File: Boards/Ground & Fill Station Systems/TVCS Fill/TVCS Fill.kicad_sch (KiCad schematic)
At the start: 109 parts, among them J1 Conn_01x01_Socket, J10 Conn_01x01_Socket, J11 Conn_01x01_Socket, J12 Conn_01x01_Socket, J13 Conn_01x01_Socket, J14 Conn_01x01_Socket, J15 Conn_01x01_Socket, J17 XT30UPB-M, J2 Conn_01x01_Socket, J3 XT30UPB-M, J4 XT30UPB-M, J5 Conn_01x01_Socket, J6 XT30UPB-M, J8 Conn_01x01_Socket, J9 Conn_01x01_Socket, Q1 2N7002H6327XTSA2, U1 MAX31856MUD+T, U10 MAX31856MUD+T, U11 IRLZ44NPBF, U12 IRLZ44NPBF, U13 LM61460AASQRJRRQ1, U14 ADS1114IRUGR, U15 TPS1120DR, U16 IRLZ44NPBF, U17 MAX485CSA+T, U3 MAX31856MUD+T, U4 PCA9306DP_118, U5 MCP9808T-E/MC, U8 TPS1120DR, U9 LM61460AASQRJRRQ1

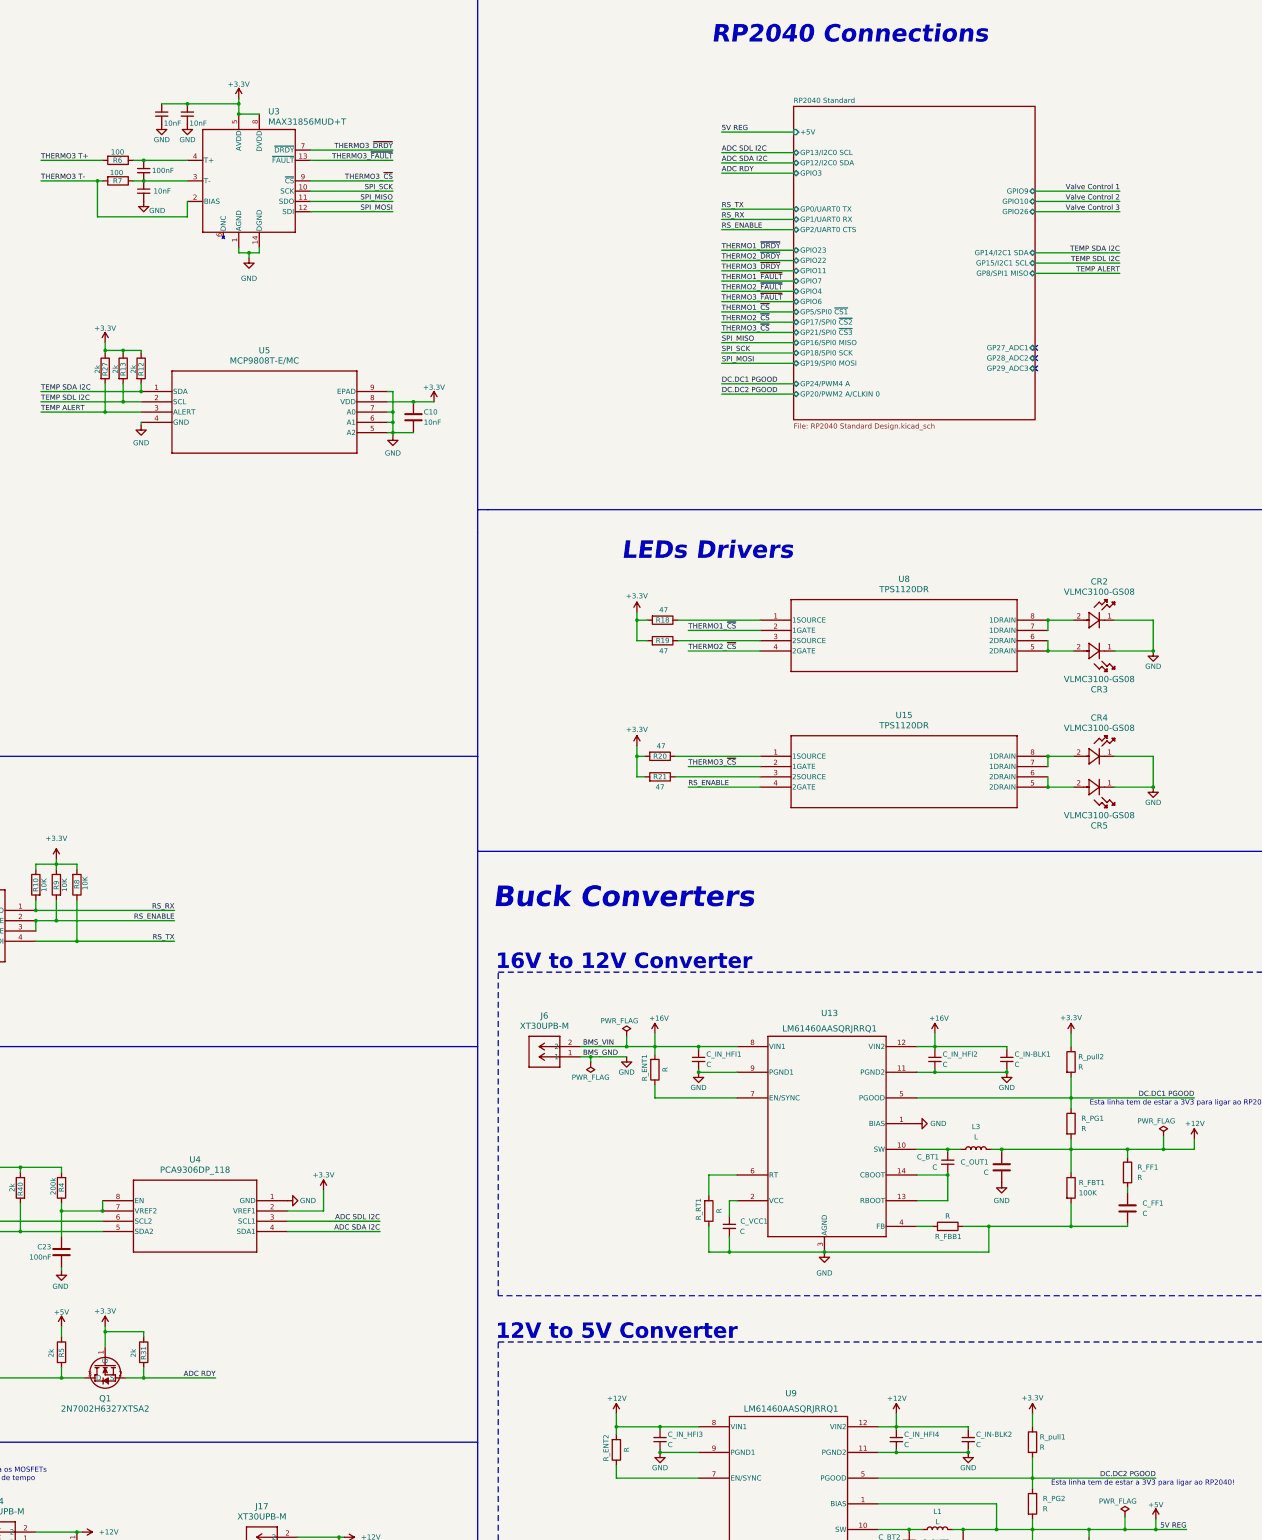
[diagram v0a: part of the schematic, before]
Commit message: Led driver circuit correction & RF FEM implementation
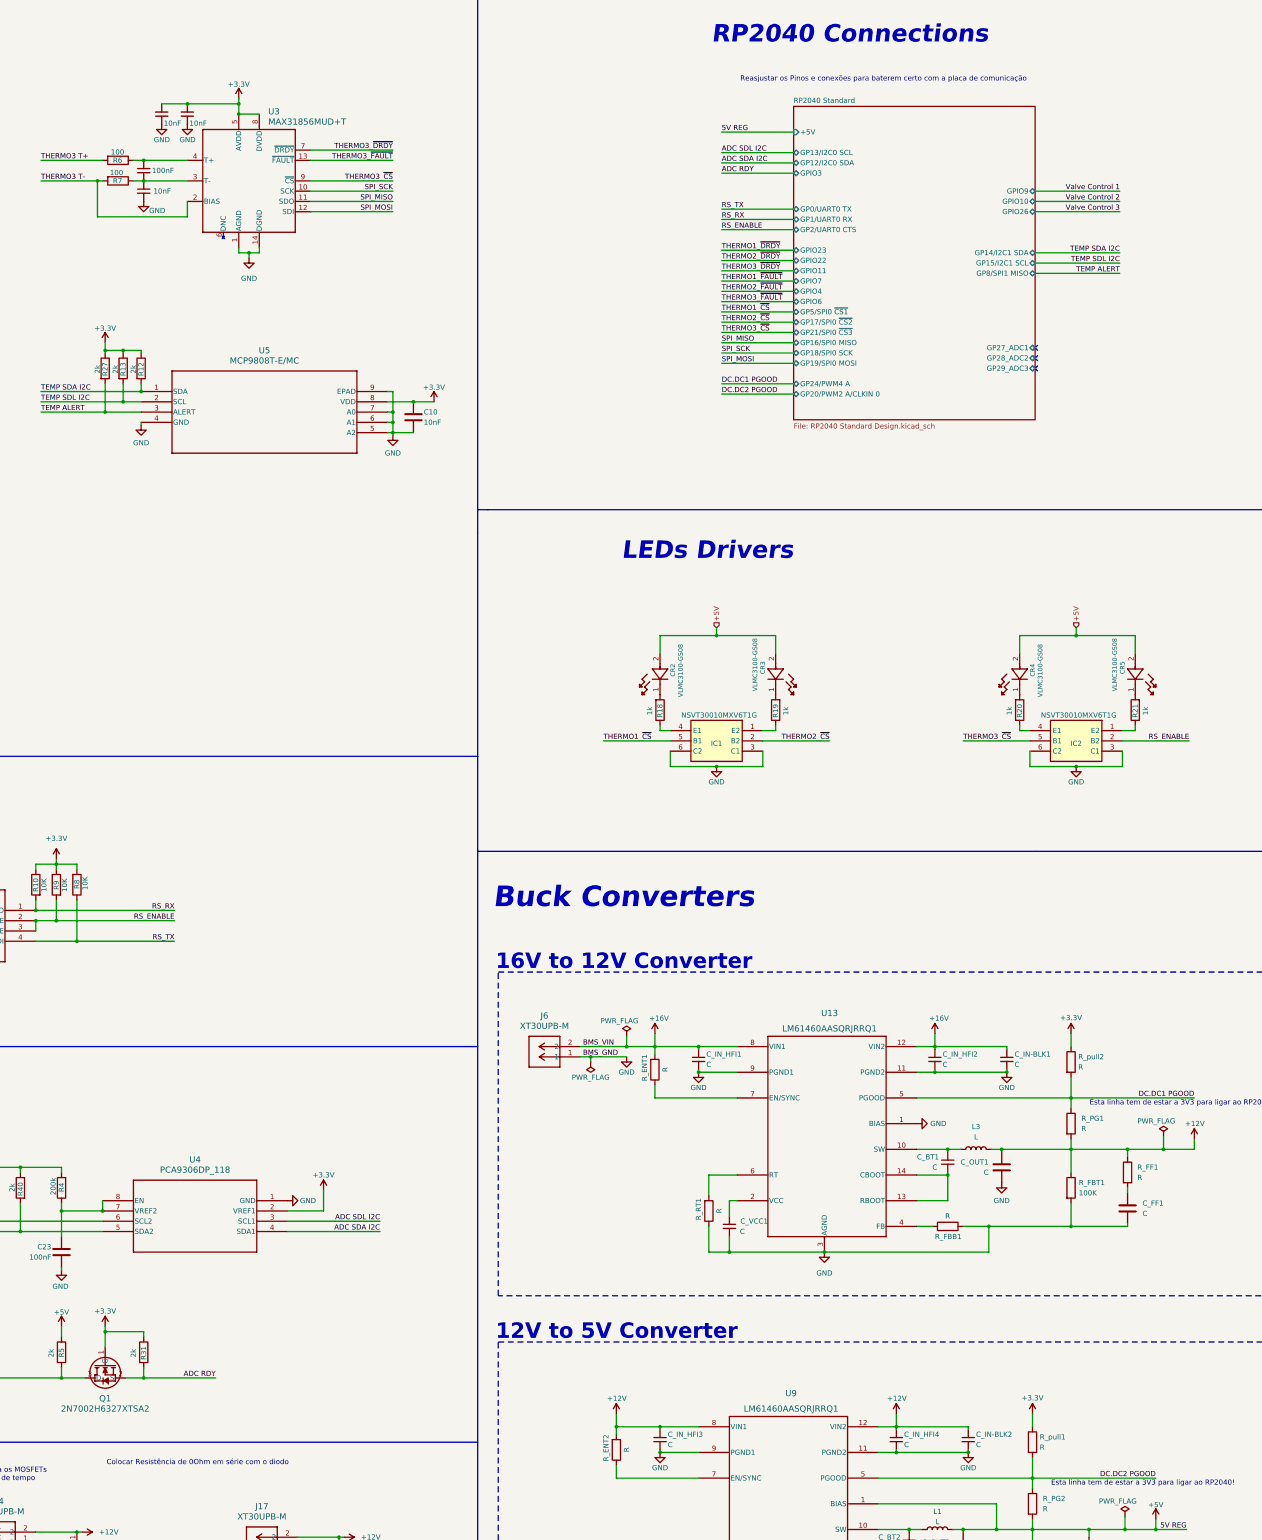
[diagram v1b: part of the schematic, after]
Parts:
- removed U15, U8: TPS1120DR, D8, symbol TPS1120DR:TPS1120DR
- added IC1, IC2: NSVT30010MXV6T1G, SOTFL50P160X60-6N, symbol NSVT30010MXV6T1G:NSVT30010MXV6T1G
- R18, R19, R20, R21: value 47 -> 1k; footprint RES_0402:RES_0402 -> RC0402N_VIS:RC0402N_VIS
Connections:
- net +3.3V: no longer R18.2, R19.2, R20.2, R21.2
- net +5V: now also CR2.2, CR3.2, CR4.2, CR5.2
- net GND: now also IC1.3 (C1), IC1.6 (C2), IC2.3 (C1), IC2.6 (C2); no longer CR2.1, CR3.1, CR4.1, CR5.1
- net RS_ENABLE: now also IC2.2 (B2)
- net THERMO1_~{CS}: now also IC1.5 (B1)
- net THERMO2_~{CS}: now also IC1.2 (B2)
- net THERMO3_~{CS}: now also IC2.5 (B1)
- net at R19.1: now also IC1.1 (E2)
- net at R21.1: now also IC2.1 (E2)
- net at R20.1: now also IC2.4 (E1)
- net at R18.1: now also IC1.4 (E1)
- new net: CR2.1, R18.2
- new net: CR3.1, R19.2
- new net: CR5.1, R21.2
- new net: CR4.1, R20.2
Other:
- note added: "Colocar Resistência de 0Ohm em série com o diodo"
- note added: "Reasjustar os Pinos e conexões para baterem certo com a placa de comunicação"

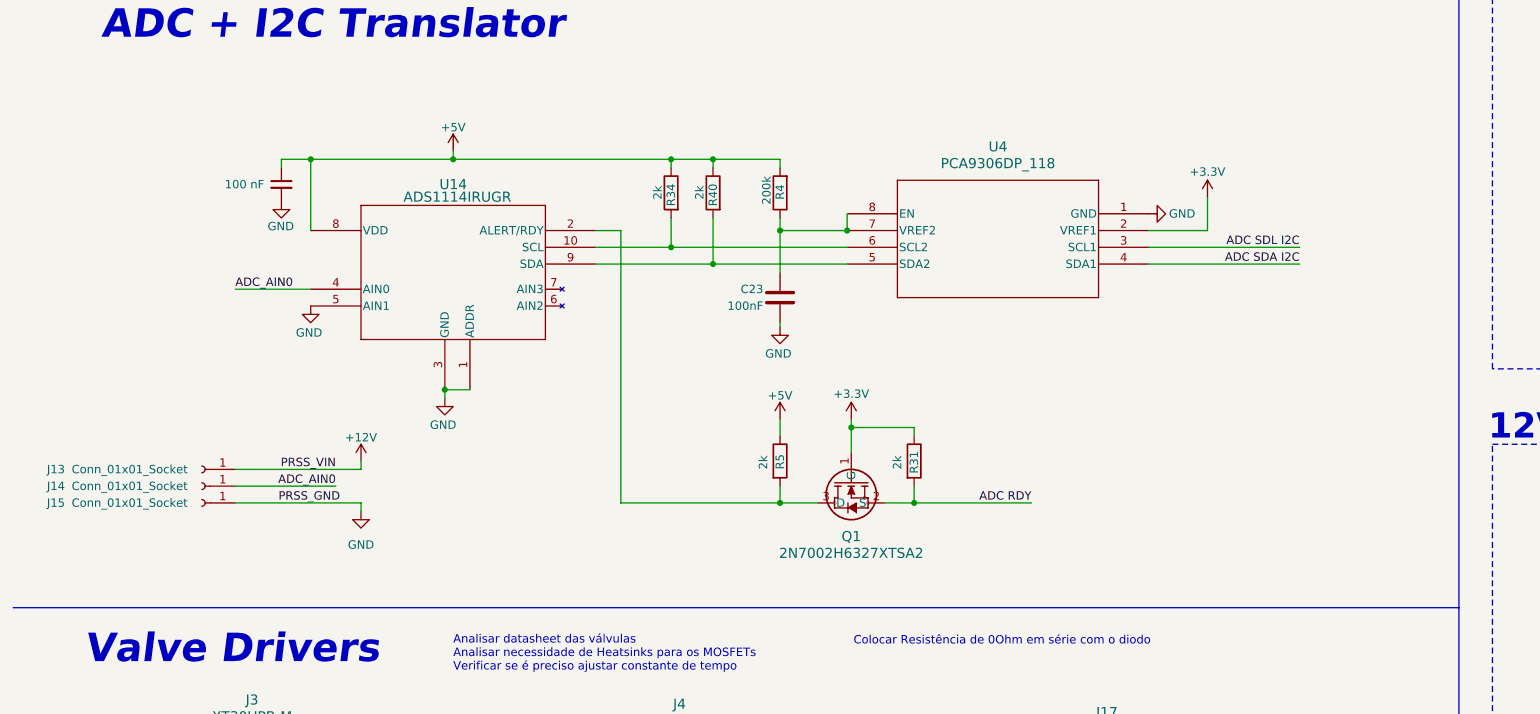
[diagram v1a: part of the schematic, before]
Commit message: ADS1115 implementation
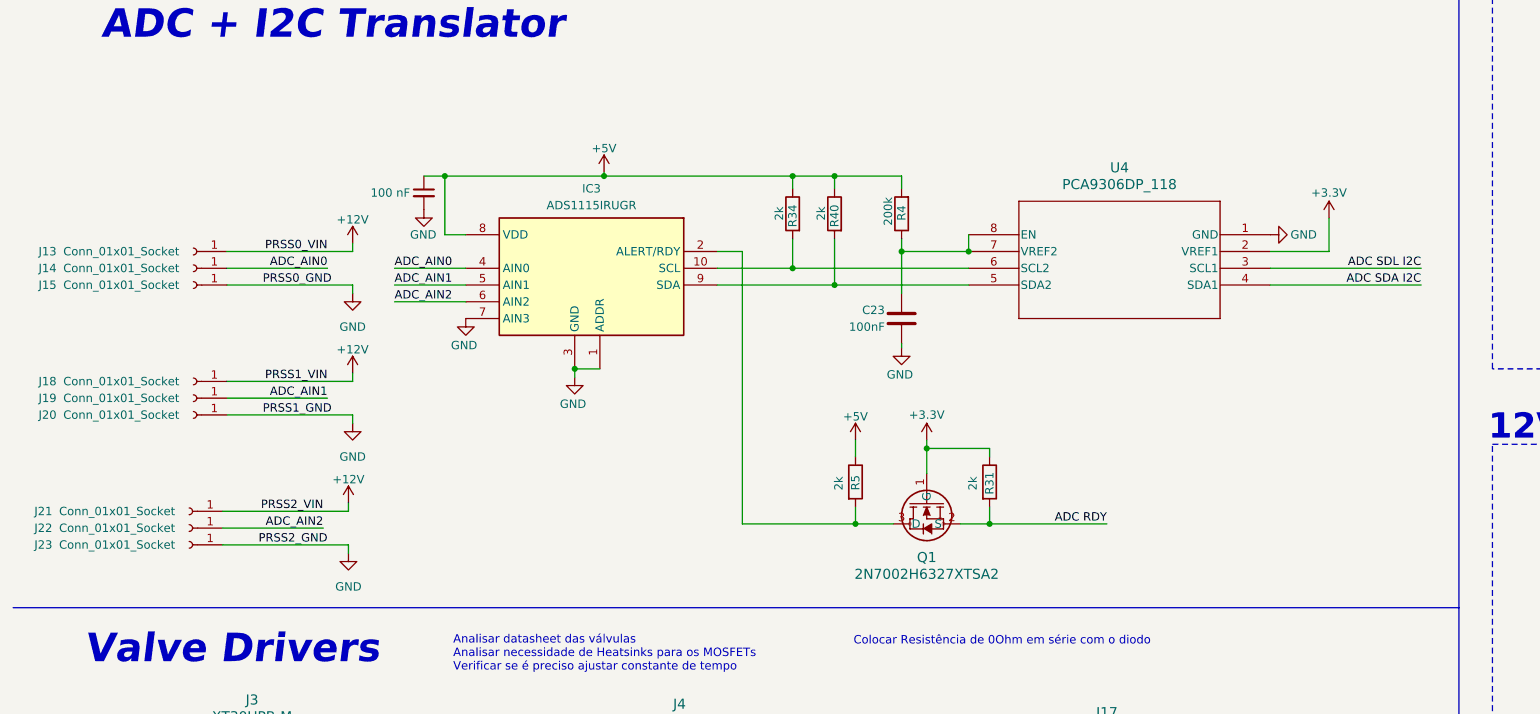
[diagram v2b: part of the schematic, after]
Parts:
- removed U14: ADS1114IRUGR, RUG10, symbol ADS1114:ADS1114IRUGR
- added IC3: ADS1115IRUGR, ADS1115IRUGR, symbol ADS1115IRUGR:ADS1115IRUGR
- added J18, J19, J20, J21, J22, J23: Conn_01x01_Socket, Button_Switch_THT:SW_Lever_1P2T_NKK_GW12LxH, symbol Connector:Conn_01x01_Socket
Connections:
- net +12V: now also J18.1 (Pin_1), J21.1 (Pin_1)
- net +5V: now also IC3.8 (VDD)
- net ADC_AIN0: now also IC3.4 (AIN0)
- net GND: now also IC3.1 (ADDR), IC3.3 (GND), IC3.7 (AIN3), J20.1 (Pin_1), J23.1 (Pin_1)
- net at R40.2, U4.5 (SDA2): now also IC3.9 (SDA)
- net at R34.2, U4.6 (SCL2): now also IC3.10 (SCL)
- net at Q1.3 (D), R5.2: now also IC3.2 (ALERT/RDY)
- new net ADC_AIN1: IC3.5 (AIN1), J19.1 (Pin_1)
- new net ADC_AIN2: IC3.6 (AIN2), J22.1 (Pin_1)
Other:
- moved on the sheet: C23, J13, J14, J15, Q1, R31, R34, R4, R40, R5, U4

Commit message: Connectors RS e ADC
Connectors nas TVCS e no OBC
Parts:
- removed J13, J14, J15, J18, J19, J2, J20, J21, J22, J23, J5: Conn_01x01_Socket, Button_Switch_THT:SW_Lever_1P2T_NKK_GW12LxH, symbol Connector:Conn_01x01_Socket
- added J13, J14, J5: 1190298, LPT Conn 3 Entradas:1190298, symbol 1190298:1190298
- added J2: 1190297, 1190297, symbol 1190297:1190297
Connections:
- net +12V: now also J13.1, J13.2, J14.1, J14.2, J5.1, J5.2
- net ADC_AIN0: now also J5.3, J5.4
- net ADC_AIN1: now also J13.3, J13.4
- net ADC_AIN2: now also J14.3, J14.4
- net GND: now also J13.5, J13.6, J14.5, J14.6, J5.5, J5.6
- net at R15.1, R16.1, U17.7 (B): now also J2.1 (1.1), J2.2 (1.2)
- net at R11.2, R16.2, U17.6 (A): now also J2.3 (2.1), J2.4 (2.2)
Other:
- moved on the sheet: C10, C23, CR2, CR4, C_BT1, C_FF1, C_IN-BLK2, C_IN_HFI3, C_IN_HFI4, C_OUT2, C_VCC1, C_VCC2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

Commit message: Mais Sockets Pico
TVCS Top, Bottom and Fill and G&F COMMS
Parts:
- added J15, J18, J19: Conn_01x01_Socket, Pico_Conn1x1:Pico_01pin, symbol Connector:Conn_01x01_Socket
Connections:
- net RP2040 Standard/GP27_ADC1: now also J15.1 (Pin_1)
- net RP2040 Standard/GP28_ADC2: now also J18.1 (Pin_1)
- net RP2040 Standard/GP29_ADC3: now also J19.1 (Pin_1)
- no-connect marks 3 -> 0
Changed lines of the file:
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@@
 		(color 0 0 0 0)
 	)
-	(no_connect
-		(at 369.57 99.06)
-	)
-	(no_connect
-		(at 369.57 104.14)
-	)
-	(no_connect
-		(at 369.57 101.6)
-	)
 	(wire
 		(pts
@@
 	(wire
 		(pts
+			(xy 369.57 101.6) (xy 379.73 101.6)
+		)
+		(stroke
+			(width 0)
+			(type default)
+		)
+	)
+	(wire
+		(pts
 			(xy 58.42 240.03) (xy 58.42 234.95)
 		)
@@
 	(wire
 		(pts
+			(xy 369.57 104.14) (xy 379.73 104.14)
+		)
+		(stroke
+			(width 0)
+			(type default)
+		)
+	)
+	(wire
+		(pts
 			(xy 143.51 99.06) (xy 148.59 99.06)
 		)
@@
 	(wire
 		(pts
+			(xy 369.57 99.06) (xy 379.73 99.06)
+		)
+		(stroke
+			(width 0)
+			(type default)
+		)
+	)
+	(wire
+		(pts
 			(xy 109.22 62.23) (xy 88.9 62.23)
 		)
@@
 	)
 	(symbol
+		(lib_id "Connector:Conn_01x01_Socket")
+		(at 384.81 104.14 0)
+		(unit 1)
+		(exclude_from_sim no)
+		(in_bom yes)
+		(on_board yes)
+		(dnp no)
+		(property "Reference" "J19"
+			(at 386.08 102.8699 0)
+			(effects
+				(font
+					(size 1.27 1.27)
+				)
+				(justify left)
+			)
+		)
+		(property "Value" "Conn_01x01_Socket"
+			(at 390.144 104.648 0)
+			(effects
+				(font
+					(size 1.27 1.27)
+				)
+				(justify left)
+			)
+		)
+		(property "Footprint" "Pico_Conn1x1:Pico_01pin"
+			(at 384.81 104.14 0)
+			(effects
+				(font
+					(size 1.27 1.27)
+				)
+				(hide yes)
+			)
+		)
+		(property "Datasheet" "~"
+			(at 384.81 104.14 0)
+			(effects
+				(font
+					(size 1.27 1.27)
+				)
+				(hide yes)
+			)
+		)
+		(property "Description" "Generic connector, single row, 01x01, script generated"
+			(at 384.81 104.14 0)
+			(effects
+				(font
+					(size 1.27 1.27)
+				)
+				(hide yes)
+			)
+		)
+		(pin "1"
+		)
+		(instances
+			(project "TVCS Fill"
+				(path "/2cb205da-01dc-4dd5-90f3-3844dc2f7334"
+					(reference "J19")
+					(unit 1)
+				)
+			)
+		)
+	)
+	(symbol
 		(lib_id "Device:R")
 		(at 393.7 187.96 180)
@@
 	)
 	(symbol
+		(lib_id "Connector:Conn_01x01_Socket")
+		(at 384.81 101.6 0)
+		(unit 1)
+		(exclude_from_sim no)
+		(in_bom yes)
+		(on_board yes)
+		(dnp no)
+		(property "Reference" "J18"
+			(at 386.08 100.3299 0)
+			(effects
+				(font
+					(size 1.27 1.27)
+				)
+				(justify left)
+			)
+		)
+		(property "Value" "Conn_01x01_Socket"
+			(at 390.144 102.108 0)
+			(effects
+				(font
+					(size 1.27 1.27)
+				)
+				(justify left)
+			)
+		)
+		(property "Footprint" "Pico_Conn1x1:Pico_01pin"
+			(at 384.81 101.6 0)
+			(effects
+				(font
+					(size 1.27 1.27)
+				)
+				(hide yes)
+			)
+		)
+		(property "Datasheet" "~"
+			(at 384.81 101.6 0)
+			(effects
+				(font
+					(size 1.27 1.27)
+				)
+				(hide yes)
+			)
+		)
+		(property "Description" "Generic connector, single row, 01x01, script generated"
+			(at 384.81 101.6 0)
+			(effects
+				(font
+					(size 1.27 1.27)
+				)
+				(hide yes)
+			)
+		)
+		(pin "1"
+		)
+		(instances
+			(project "TVCS Fill"
+				(path "/2cb205da-01dc-4dd5-90f3-3844dc2f7334"
+					(reference "J18")
+					(unit 1)
+				)
+			)
+		)
+	)
+	(symbol
 		(lib_id "Device:R")
 		(at 41.91 111.76 270)
@@
 	)
 	(symbol
+		(lib_id "Connector:Conn_01x01_Socket")
+		(at 384.81 99.06 0)
+		(unit 1)
+		(exclude_from_sim no)
+		(in_bom yes)
+		(on_board yes)
+		(dnp no)
+		(property "Reference" "J15"
+			(at 386.08 97.7899 0)
+			(effects
+				(font
+					(size 1.27 1.27)
+				)
+				(justify left)
+			)
+		)
+		(property "Value" "Conn_01x01_Socket"
+			(at 390.144 99.568 0)
+			(effects
+				(font
+					(size 1.27 1.27)
+				)
+				(justify left)
+			)
+		)
+		(property "Footprint" "Pico_Conn1x1:Pico_01pin"
+			(at 384.81 99.06 0)
+			(effects
+				(font
+					(size 1.27 1.27)
+				)
+				(hide yes)
+			)
+		)
+		(property "Datasheet" "~"
+			(at 384.81 99.06 0)
+			(effects
+				(font
+					(size 1.27 1.27)
+				)
+				(hide yes)
+			)
+		)
+		(property "Description" "Generic connector, single row, 01x01, script generated"
+			(at 384.81 99.06 0)
+			(effects
+				(font
+					(size 1.27 1.27)
+				)
+				(hide yes)
+			)
+		)
+		(pin "1"
+		)
+		(instances
+			(project "TVCS Fill"
+				(path "/2cb205da-01dc-4dd5-90f3-3844dc2f7334"
+					(reference "J15")
+					(unit 1)
+				)
+			)
+		)
+	)
+	(symbol
 		(lib_id "Device:C_Small")
 		(at 148.59 54.61 0)
@@
 		)
 		(pin "GP29_ADC3" bidirectional
-			(at 369.57 104.775 0)
+			(at 369.57 104.14 0)
 			(effects
 				(font
@@
 		)
 		(pin "GP27_ADC1" bidirectional
-			(at 369.57 99.695 0)
+			(at 369.57 99.06 0)
 			(effects
 				(font
@@
 		)
 		(pin "GP28_ADC2" bidirectional
-			(at 369.57 102.235 0)
+			(at 369.57 101.6 0)
 			(effects
 				(font
